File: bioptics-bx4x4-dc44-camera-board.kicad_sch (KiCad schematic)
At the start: 1 part

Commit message: Wire DRAM
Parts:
- added U?: IS4xS32160F-xTL, Package_SOP_DRAM:TSOP-II-86_22.2x10.16mm_P0.5mm, symbol Memory_RAM_ISSI:IS4xS32160F-xTL
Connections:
- net FMC_A0: now also U?.25 (A0)
- net FMC_A1: now also U?.26 (A1)
- net FMC_A10: now also U?.24 (A10)
- net FMC_A11: now also U?.21 (A11)
- net FMC_A12: now also U?.69 (A12)
- net FMC_A14: now also U?.22 (BA0)
- net FMC_A15: now also U?.23 (BA1)
- net FMC_A2: now also U?.27 (A2)
- net FMC_A3: now also U?.60 (A3)
- net FMC_A4: now also U?.61 (A4)
- net FMC_A5: now also U?.62 (A5)
- net FMC_A6: now also U?.63 (A6)
- net FMC_A7: now also U?.64 (A7)
- net FMC_A8: now also U?.65 (A8)
- net FMC_A9: now also U?.66 (A9)
- net FMC_D0: now also U?.2 (DQ0)
- net FMC_D1: now also U?.4 (DQ1)
- net FMC_D10: now also U?.77 (DQ10)
- net FMC_D11: now also U?.79 (DQ11)
- net FMC_D12: now also U?.80 (DQ12)
- net FMC_D13: now also U?.82 (DQ13)
- net FMC_D14: now also U?.83 (DQ14)
- net FMC_D15: now also U?.85 (DQ15)
- net FMC_D16: now also U?.31 (DQ16)
- net FMC_D17: now also U?.33 (DQ17)
- net FMC_D18: now also U?.34 (DQ18)
- net FMC_D19: now also U?.36 (DQ19)
- net FMC_D2: now also U?.5 (DQ2)
- net FMC_D20: now also U?.37 (DQ20)
- net FMC_D21: now also U?.39 (DQ21)
- net FMC_D22: now also U?.40 (DQ22)
- net FMC_D23: now also U?.42 (DQ23)
- net FMC_D24: now also U?.45 (DQ24)
- net FMC_D25: now also U?.47 (DQ25)
- net FMC_D26: now also U?.48 (DQ26)
- net FMC_D27: now also U?.50 (DQ27)
- net FMC_D28: now also U?.51 (DQ28)
- net FMC_D29: now also U?.53 (DQ29)
- net FMC_D3: now also U?.7 (DQ3)
- net FMC_D30: now also U?.54 (DQ30)
- net FMC_D31: now also U?.56 (DQ31)
- net FMC_D4: now also U?.8 (DQ4)
- net FMC_D5: now also U?.10 (DQ5)
- net FMC_D6: now also U?.11 (DQ6)
- net FMC_D7: now also U?.13 (DQ7)
- net FMC_D8: now also U?.74 (DQ8)
- net FMC_D9: now also U?.76 (DQ9)
- net FMC_NBL0: now also U?.16 (DQM0)
- net FMC_NBL1: now also U?.71 (DQM1)
- net FMC_NBL2: now also U?.28 (DQM2)
- net FMC_NBL3: now also U?.59 (DQM3)
- net FMC_SDCKE0: now also U?.67 (CKE); no longer U?.35 (PC3_C)
- net FMC_SDCKE1: no longer U?.163 (PB5)
- net FMC_SDCLK: now also U?.68 (CLK)
- net FMC_SDNCAS: now also U?.18 (~{CAS})
- net FMC_SDNE0: now also U?.20 (~{CS}); no longer U?.34 (PC2_C)
- net FMC_SDNRAS: now also U?.19 (~{RAS})
- net FMC_SDNWE: now also U?.17 (~{WE}); no longer U?.32 (PC0)
- net ULPI_DIR: now reaches U?.13 (PI11)
- net ULPI_DIR: now also U?.34 (PC2_C)
- net ULPI_NXT: now reaches U?.45 (PH4)
- net ULPI_NXT: now also U?.35 (PC3_C)
- net ULPI_D0: now reaches U?.47 (PA3)
- net SOF: now reaches U?.50 (PA4)
- net ULPI_CK: now reaches U?.51 (PA5)
- net ULPI_D1: now reaches U?.56 (PB0)
- net ULPI_D2: now reaches U?.57 (PB1)
- net ULPI_D3: now reaches U?.79 (PB10)
- net ULPI_D4: now reaches U?.80 (PB11)
- net ULPI_D5: now reaches U?.92 (PB12)
- net ULPI_D6: now reaches U?.93 (PB13)
- new net ULPI_D7: U?.163 (PB5)
- new net ULPI_STP: U?.32 (PC0)
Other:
- note added: "TODO: - Check SDRAM pinout against datasheet"

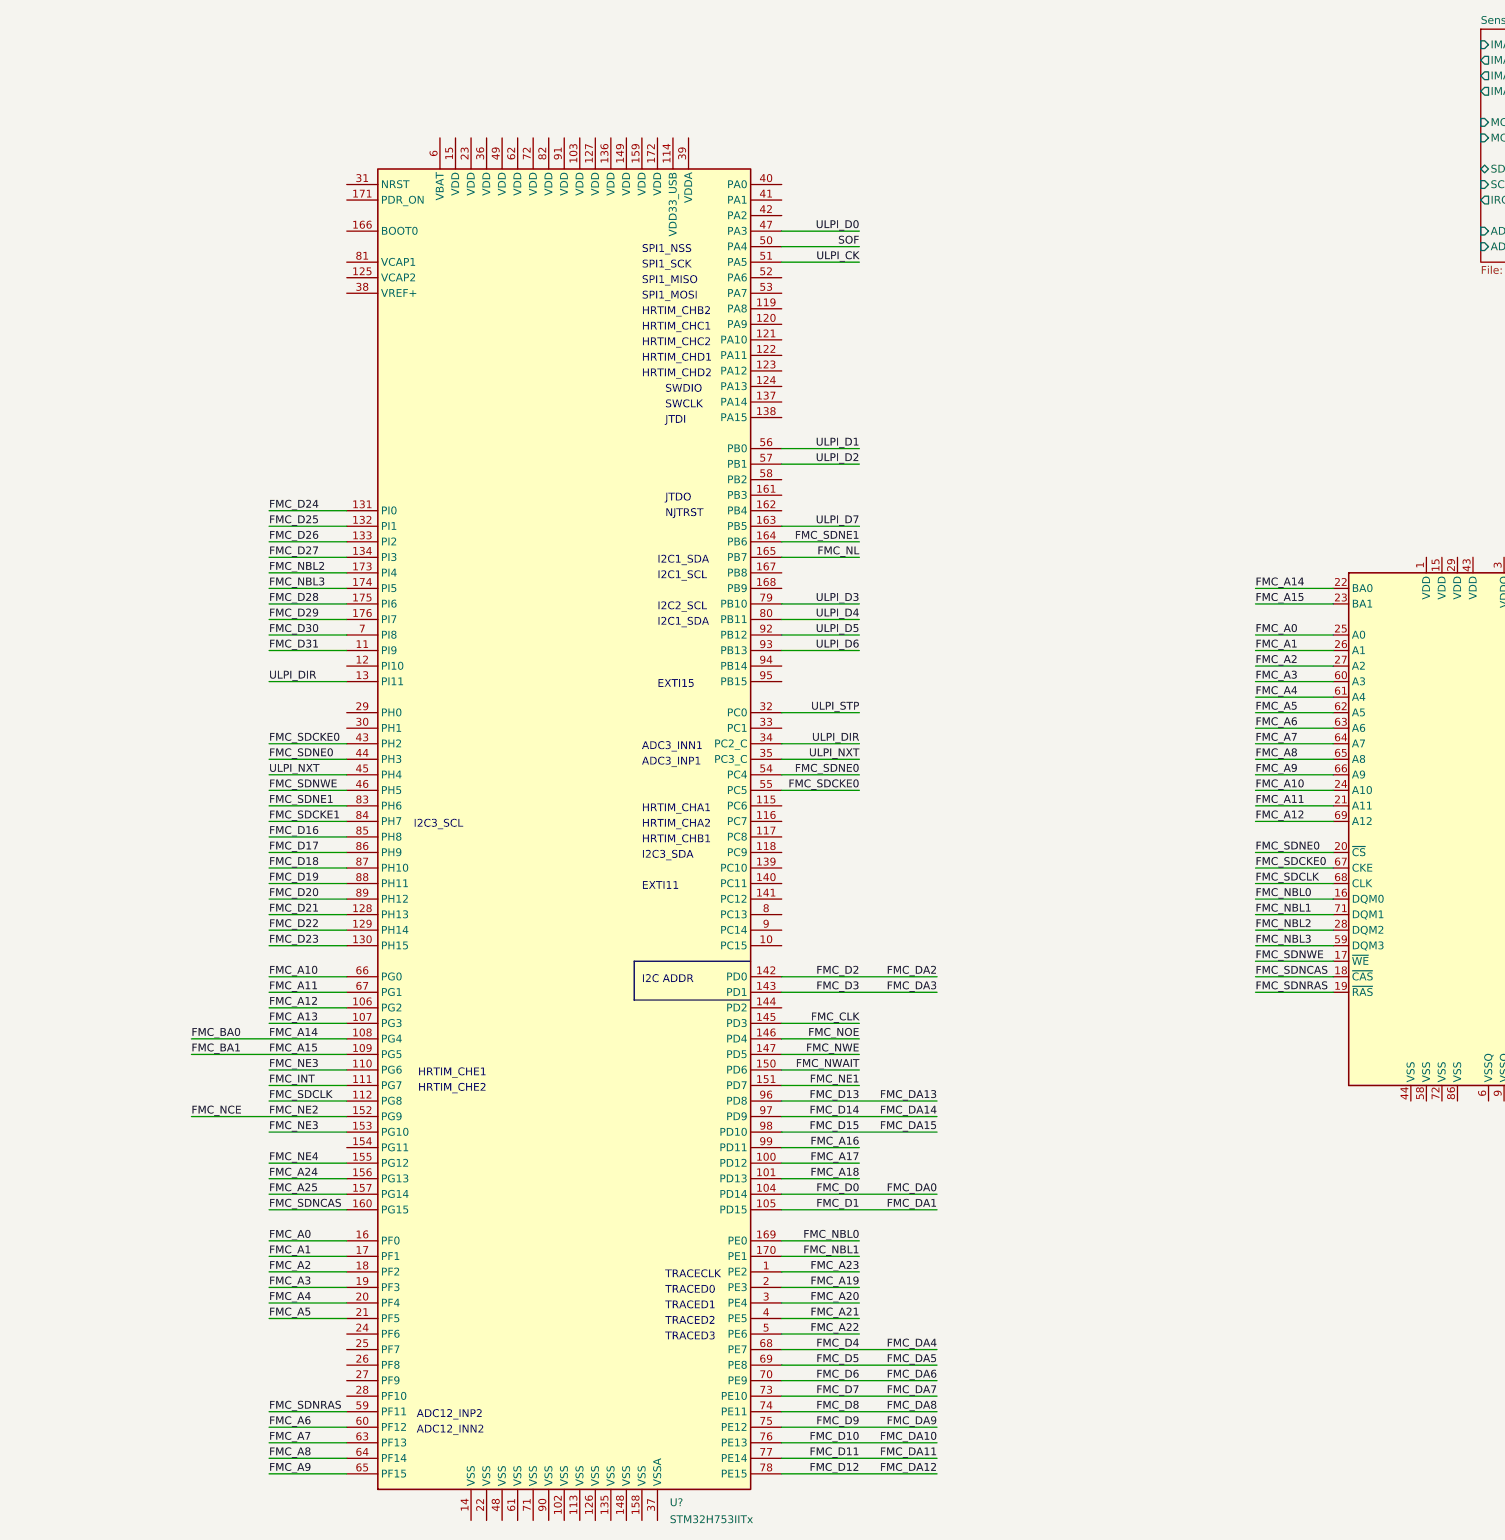
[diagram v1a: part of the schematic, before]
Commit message: Map out available SPIs
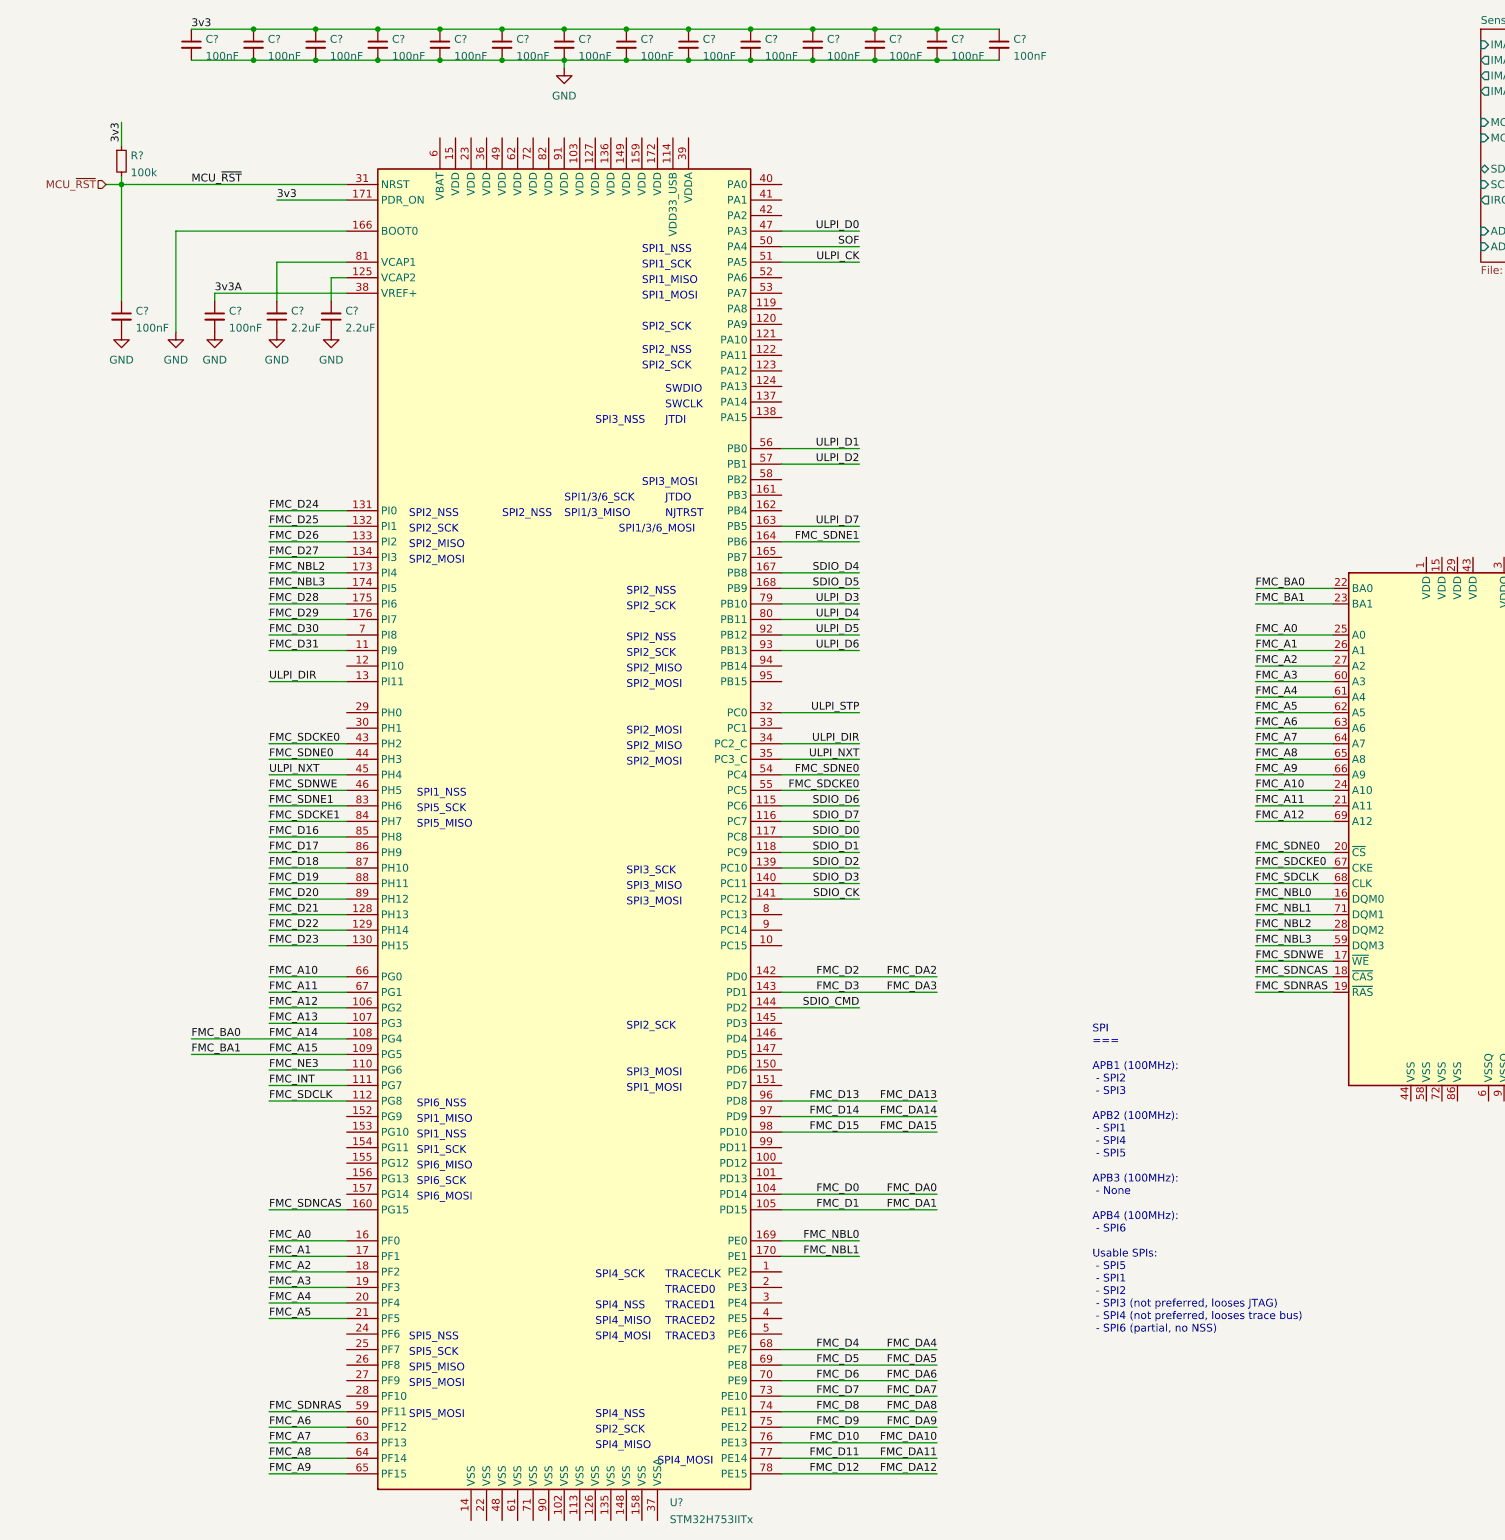
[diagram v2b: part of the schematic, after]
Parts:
- added C? (x16): 100nF, Capacitor_SMD:C_0402_1005Metric, symbol Device:C_Small
- added C? (x2): 2.2uF, Capacitor_SMD:C_0402_1005Metric, symbol Device:C_Small
- added R?: 100k, Resistor_SMD:R_0402_1005Metric, symbol Device:R_Small
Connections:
- net FMC_NE3: no longer U?.153 (PG10)
- net SDIO_D6: now reaches U?.115 (PC6)
- net SDIO_D7: now reaches U?.116 (PC7)
- net SDIO_D0: now reaches U?.117 (PC8)
- net SDIO_D1: now reaches U?.118 (PC9)
- net at U?.125 (VCAP2): now also C?.2
- net SDIO_D2: now reaches U?.139 (PC10)
- net SDIO_D3: now reaches U?.140 (PC11)
- net SDIO_CK: now reaches U?.141 (PC12)
- net SDIO_CMD: now reaches U?.144 (PD2)
- net GND: now reaches U?.166 (BOOT0)
- net GND: now also C?.1, C?.1, C?.2, C?.2, C?.2, C?.2, C?.2, C?.2, C?.2, C?.2, C?.2, C?.2, C?.2, C?.2, C?.2, C?.2, C?.2, C?.2
- net SDIO_D4: now reaches U?.167 (PB8)
- net SDIO_D5: now reaches U?.168 (PB9)
- net 3v3: now reaches U?.171 (PDR_ON)
- net 3v3: now also C?.1, C?.1, C?.1, C?.1, C?.1, C?.1, C?.1, C?.1, C?.1, C?.1, C?.1, C?.1, C?.1, C?.1, R?.1
- net MCU_~{RST}: now reaches U?.31 (NRST)
- net MCU_~{RST}: now also C?.1, R?.2
- net 3v3A: now reaches U?.38 (VREF+)
- net 3v3A: now also C?.1
- net at U?.81 (VCAP1): now also C?.2
- net FMC_A16: no longer names the net of U?.99 (PD11)
- net FMC_A17: no longer names the net of U?.100 (PD12)
- net FMC_A18: no longer names the net of U?.101 (PD13)
- net FMC_A19: no longer names the net of U?.2 (PE3)
- net FMC_A20: no longer names the net of U?.3 (PE4)
- net FMC_A21: no longer names the net of U?.4 (PE5)
- net FMC_A22: no longer names the net of U?.5 (PE6)
- net FMC_A23: no longer names the net of U?.1 (PE2)
- net FMC_A24: no longer names the net of U?.156 (PG13)
- net FMC_A25: no longer names the net of U?.157 (PG14)
- net FMC_CLK: no longer names the net of U?.145 (PD3)
- net FMC_NCE: no longer names the net of U?.152 (PG9)
- net FMC_NE1: no longer names the net of U?.151 (PD7)
- net FMC_NE4: no longer names the net of U?.155 (PG12)
- net FMC_NL: no longer names the net of U?.165 (PB7)
- net FMC_NOE: no longer names the net of U?.146 (PD4)
- net FMC_NWAIT: no longer names the net of U?.150 (PD6)
- net FMC_NWE: no longer names the net of U?.147 (PD5)
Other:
- note added: "SPI === APB1 (100MHz): - SPI2 - SPI3 APB2 (100MHz): - SPI1 - SPI4 - SPI5 APB3 (100MHz): - None APB4 (100MHz): - SPI6 Usable SPIs: - SPI5 - SPI1 - SPI2 - SPI3 (not preferred, looses JTAG) - SPI4 (not preferred, looses trace bus) - SPI6 (partial, no NSS)"
- note added: "SPI1/3/6_MOSI"
- note added: "SPI1/3/6_SCK"
- note added: "SPI1/3_MISO"
- note added: "SPI2_MISO"
- note added: "SPI2_MOSI"
- note added: "SPI2_NSS"
- note added: "SPI2_SCK"
- note added: "SPI3_MISO"
- note added: "SPI3_MOSI"
- note added: "SPI3_NSS"
- note added: "SPI3_SCK"
- note added: "SPI4_MISO"
- note added: "SPI4_MOSI"
- note added: "SPI4_NSS"
- note added: "SPI4_SCK"
- note added: "SPI5_MISO"
- note added: "SPI5_MOSI"
- note added: "SPI5_NSS"
- note added: "SPI5_SCK"
- note added: "SPI6_MISO"
- note added: "SPI6_MOSI"
- note added: "SPI6_NSS"
- note added: "SPI6_SCK"
- note removed: "ADC12_INN2"
- note removed: "ADC12_INP2"
- note removed: "ADC3_INN1"
- note removed: "ADC3_INP1"
- note removed: "EXTI11"
- note removed: "EXTI15"
- note removed: "HRTIM_CHA1"
- note removed: "HRTIM_CHA2"
- note removed: "HRTIM_CHB1"
- note removed: "HRTIM_CHB2"
- note removed: "HRTIM_CHC1"
- note removed: "HRTIM_CHC2"
- note removed: "HRTIM_CHD1"
- note removed: "HRTIM_CHD2"
- note removed: "HRTIM_CHE1"
- note removed: "HRTIM_CHE2"
- note removed: "I2C ADDR"
- note removed: "I2C1_SCL"
- note removed: "I2C1_SDA"
- note removed: "I2C2_SCL"
- note removed: "I2C3_SCL"
- note removed: "I2C3_SDA"

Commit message: Eliminate duplicate MCU signals
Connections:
- net FMC_SDCKE0: no longer U?.55 (PC5)
- net FMC_SDNE0: no longer U?.54 (PC4)
- net FMC_SDNE1: no longer U?.164 (PB6)
- net ULPI_DIR: no longer U?.34 (PC2_C)
- net ULPI_NXT: no longer U?.35 (PC3_C)
- net FMC_INT: no longer names the net of U?.111 (PG7)
- net FMC_NE3: no longer names the net of U?.110 (PG6)
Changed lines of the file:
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@@
-    (stroke (width 0) (type default) (color 0 0 0 0))
-  )
-  (wire (pts (xy 119.38 190.5) (xy 132.08 190.5))
     (stroke (width 0) (type default) (color 0 0 0 0))
   )
@@
     (stroke (width 0) (type default) (color 0 0 0 0))
   )
-  (wire (pts (xy 215.9 137.16) (xy 203.2 137.16))
-    (stroke (width 0) (type default) (color 0 0 0 0))
-  )
-  (wire (pts (xy 215.9 101.6) (xy 203.2 101.6))
-    (stroke (width 0) (type default) (color 0 0 0 0))
-  )
   (wire (pts (xy 203.2 160.02) (xy 215.9 160.02))
     (stroke (width 0) (type default) (color 0 0 0 0))
@@
     (stroke (width 0) (type default) (color 0 0 0 0))
   )
-  (wire (pts (xy 215.9 139.7) (xy 203.2 139.7))
-    (stroke (width 0) (type default) (color 0 0 0 0))
-  )
   (wire (pts (xy 167.64 22.86) (xy 177.8 22.86))
     (stroke (width 0) (type default) (color 0 0 0 0))
@@
     (stroke (width 0) (type default) (color 0 0 0 0))
   )
-  (wire (pts (xy 215.9 134.62) (xy 203.2 134.62))
-    (stroke (width 0) (type default) (color 0 0 0 0))
-  )
   (wire (pts (xy 119.38 119.38) (xy 132.08 119.38))
     (stroke (width 0) (type default) (color 0 0 0 0))
@@
     (stroke (width 0) (type default) (color 0 0 0 0))
   )
-  (wire (pts (xy 119.38 187.96) (xy 132.08 187.96))
-    (stroke (width 0) (type default) (color 0 0 0 0))
-  )
   (wire (pts (xy 106.68 22.86) (xy 116.84 22.86))
     (stroke (width 0) (type default) (color 0 0 0 0))
@@
   )
   (wire (pts (xy 351.79 144.78) (xy 364.49 144.78))
-    (stroke (width 0) (type default) (color 0 0 0 0))
-  )
-  (wire (pts (xy 215.9 142.24) (xy 203.2 142.24))
     (stroke (width 0) (type default) (color 0 0 0 0))
   )
@@
     (effects (font (size 1.27 1.27)) (justify left bottom))
   )
-  (label "FMC_INT" (at 119.38 190.5 0)
-    (effects (font (size 1.27 1.27)) (justify left bottom))
-  )
   (label "FMC_A1" (at 119.38 218.44 0)
     (effects (font (size 1.27 1.27)) (justify left bottom))
@@
     (effects (font (size 1.27 1.27)) (justify right bottom))
   )
-  (label "ULPI_DIR" (at 215.9 134.62 180)
-    (effects (font (size 1.27 1.27)) (justify right bottom))
-  )
   (label "FMC_SDNE1" (at 119.38 144.78 0)
     (effects (font (size 1.27 1.27)) (justify left bottom))
   )
-  (label "FMC_SDNE0" (at 215.9 139.7 180)
-    (effects (font (size 1.27 1.27)) (justify right bottom))
-  )
   (label "ULPI_D3" (at 215.9 111.76 180)
     (effects (font (size 1.27 1.27)) (justify right bottom))
@@
     (effects (font (size 1.27 1.27)) (justify right bottom))
   )
-  (label "FMC_NE3" (at 119.38 187.96 0)
-    (effects (font (size 1.27 1.27)) (justify left bottom))
-  )
   (label "FMC_D11" (at 215.9 251.46 180)
     (effects (font (size 1.27 1.27)) (justify right bottom))
   )
-  (label "FMC_SDNE1" (at 215.9 101.6 180)
-    (effects (font (size 1.27 1.27)) (justify right bottom))
-  )
   (label "FMC_A15" (at 119.38 185.42 0)
     (effects (font (size 1.27 1.27)) (justify left bottom))
@@
     (effects (font (size 1.27 1.27)) (justify left bottom))
   )
-  (label "FMC_SDCKE0" (at 215.9 142.24 180)
-    (effects (font (size 1.27 1.27)) (justify right bottom))
-  )
   (label "FMC_D19" (at 119.38 157.48 0)
     (effects (font (size 1.27 1.27)) (justify left bottom))
@@
     (effects (font (size 1.27 1.27)) (justify left bottom))
   )
-  (label "ULPI_NXT" (at 215.9 137.16 180)
-    (effects (font (size 1.27 1.27)) (justify right bottom))
-  )
   (label "FMC_D28" (at 364.49 180.34 180)
